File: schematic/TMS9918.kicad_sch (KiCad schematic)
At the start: 23 parts, among them J1 Bus, J2 Video out, J3 Power, J4 ext, Q1 2N4401, U1 TMS9918A, U2 HM62256BLP, U3 74HCT574, U4 74HCT574, U5 74HCT574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

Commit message: V1.1
Various improvements
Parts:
- removed A1: Arduino_Nano_v3.x, Module:Arduino_Nano, symbol MCU_Module:Arduino_Nano_v3.x
- removed C9: 0.1uf, Capacitor_THT:C_Disc_D3.0mm_W1.6mm_P2.50mm, symbol Device:C
- added R1: (no value), symbol Device:R
- C7, C8: value (none) -> 22pf
- J1: value Bus -> (none); footprint Connector_PinHeader_2.54mm:PinHeader_1x12_P2.54mm_Vertical -> (none)
- J4: value ext -> (none); footprint Connector_PinHeader_2.54mm:PinHeader_1x04_P2.54mm_Vertical -> (none)
- Q1: value 2N4401 -> (none); footprint Package_TO_SOT_THT:TO-92 -> (none)
- R3: value 470 -> (none)
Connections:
- net D0: now also U1.24 (CD0); no longer U1.17 (CD7)
- net D1: now also U1.23 (CD1); no longer U1.18 (CD6)
- net D2: now also U1.22 (CD2); no longer U1.19 (CD5)
- net D3: now also U1.21 (CD3); no longer U1.20 (CD4)
- net D4: now also U1.20 (CD4); no longer U1.21 (CD3)
- net D5: now also U1.19 (CD5); no longer U1.22 (CD2)
- net D6: now also U1.18 (CD6); no longer U1.23 (CD1)
- net D7: now also U1.17 (CD7); no longer U1.24 (CD0)
- net GND: now also R1.2
- net at J2.2 (Pin_2), Q1.1 (E): now also R1.1
- net COMVID renamed vid
- net CPUCLK: no longer names the net of J4.4 (Pin_4), U1.38 (CPUCLK)
- net EXTVDP renamed EXT
- net GROMCLK: no longer names the net of J4.3 (Pin_3), U1.37 (GROMCLK)
- net ~{INT}: no longer names the net of U1.16 (~{INT})
- no-connect marks 9 -> 5
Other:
- moved on the sheet: C2, C3, C4, C5, C6, U2, U3, U4, U5, U6D, U6E, U6F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

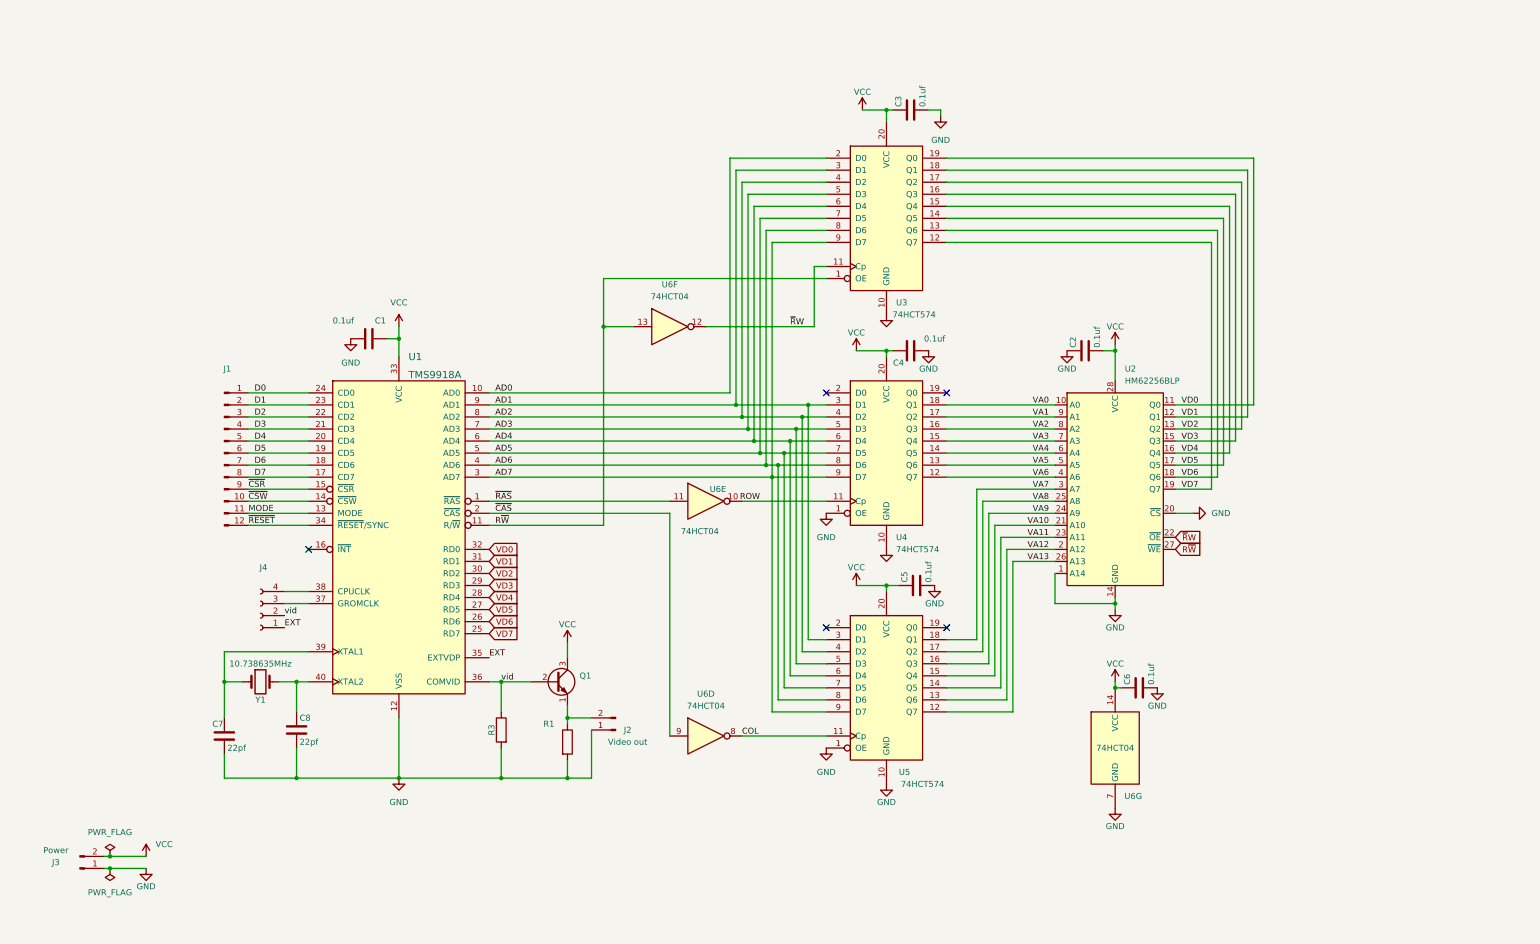
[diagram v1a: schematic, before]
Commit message: V1.2
Label D0..D7 order changed
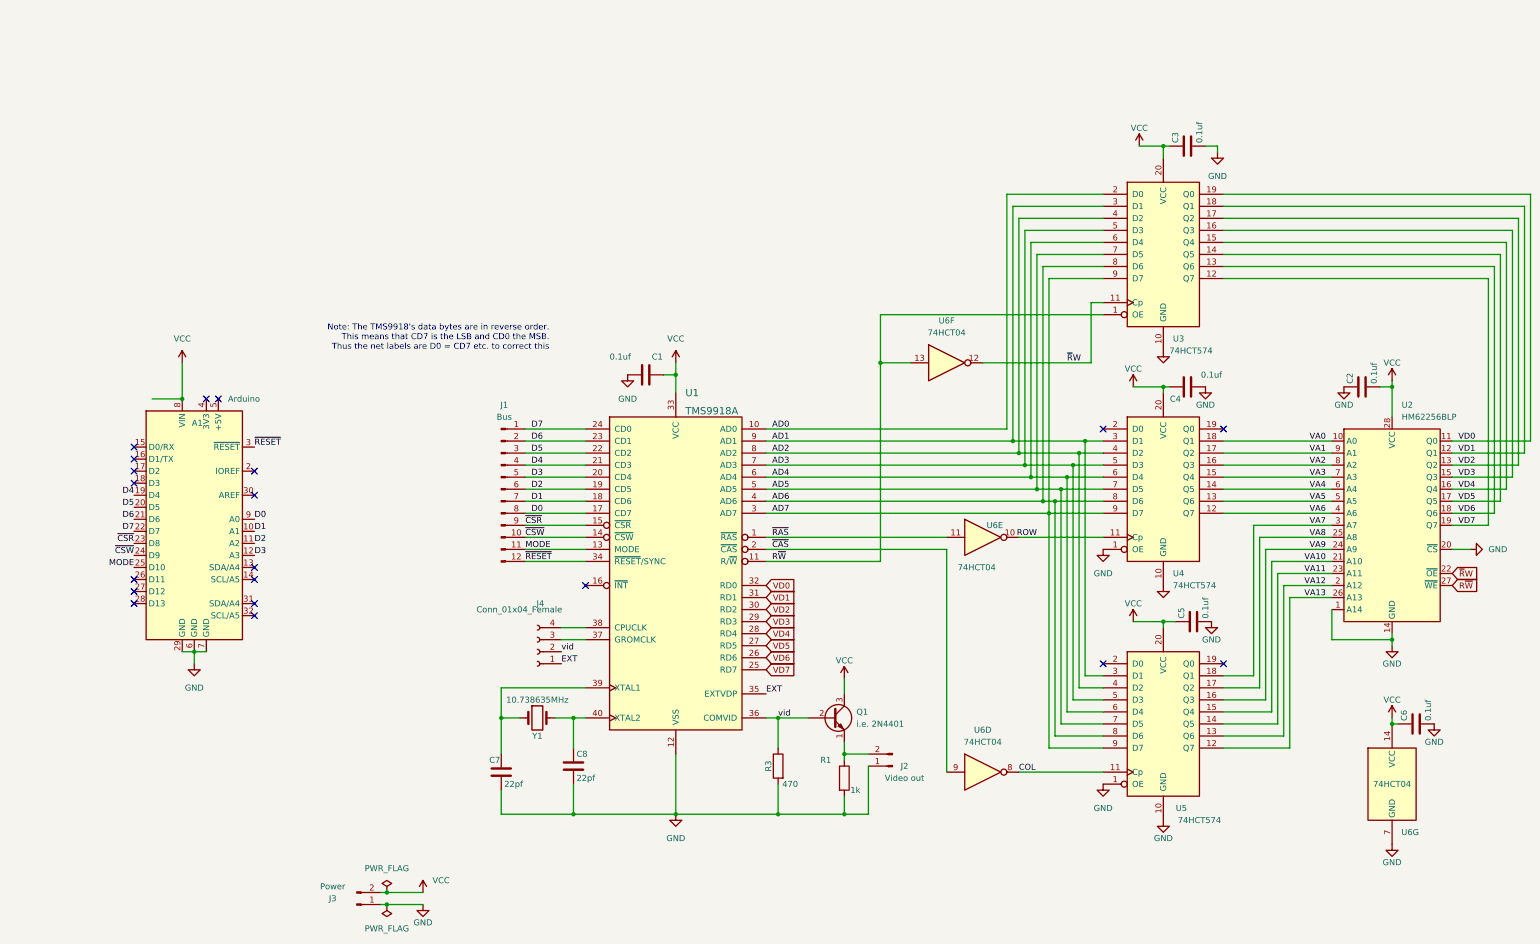
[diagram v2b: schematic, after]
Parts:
- added A1: Arduino, Module:Arduino_UNO_R3, symbol MCU_Module:Arduino_UNO_R3
- J1: value (none) -> Bus; footprint (none) -> Connector_PinHeader_2.54mm:PinHeader_1x12_P2.54mm_Vertical
- J4: value (none) -> Conn_01x04_Female; footprint (none) -> Connector_PinHeader_2.54mm:PinHeader_1x04_P2.54mm_Vertical
- Q1: value (none) -> i.e. 2N4401; footprint (none) -> Package_TO_SOT_THT:TO-92
- R1: value (none) -> 1k; footprint (none) -> Resistor_THT:R_Axial_DIN0207_L6.3mm_D2.5mm_P7.62mm_Horizontal
- R3: value (none) -> 470
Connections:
- net D0: now also J1.8 (Pin_8), U1.17 (CD7), A1.9 (A0); no longer J1.1 (Pin_1), U1.24 (CD0)
- net D1: now also J1.7 (Pin_7), U1.18 (CD6), A1.10 (A1); no longer J1.2 (Pin_2), U1.23 (CD1)
- net D2: now also J1.6 (Pin_6), U1.19 (CD5), A1.11 (A2); no longer J1.3 (Pin_3), U1.22 (CD2)
- net D3: now also J1.5 (Pin_5), U1.20 (CD4), A1.12 (A3); no longer J1.4 (Pin_4), U1.21 (CD3)
- net D4: now also J1.4 (Pin_4), U1.21 (CD3), A1.19 (D4); no longer J1.5 (Pin_5), U1.20 (CD4)
- net D5: now also J1.3 (Pin_3), U1.22 (CD2), A1.20 (D5); no longer J1.6 (Pin_6), U1.19 (CD5)
- net D6: now also J1.2 (Pin_2), U1.23 (CD1), A1.21 (D6); no longer J1.7 (Pin_7), U1.18 (CD6)
- net D7: now also J1.1 (Pin_1), U1.24 (CD0), A1.22 (D7); no longer J1.8 (Pin_8), U1.17 (CD7)
- net GND: now also A1.29 (GND), A1.6 (GND), A1.7 (GND)
- net MODE: now also A1.25 (D10)
- net VCC: now also A1.8 (VIN)
- net ~{CSR}: now also A1.23 (D8)
- net ~{CSW}: now also A1.24 (D9)
- net ~{RESET}: now also A1.3 (~{RESET})
- no-connect marks 5 -> 20
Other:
- note added: "Note: The TMS9918's data bytes are in reverse order. This means that CD7 is the LSB and CD0 the MSB. Thus the net labels are D0 = CD7 etc. to correct this"
- moved on the sheet: C1, C2, C3, C4, C5, C6, C7, C8, J1, J2, J3, J4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

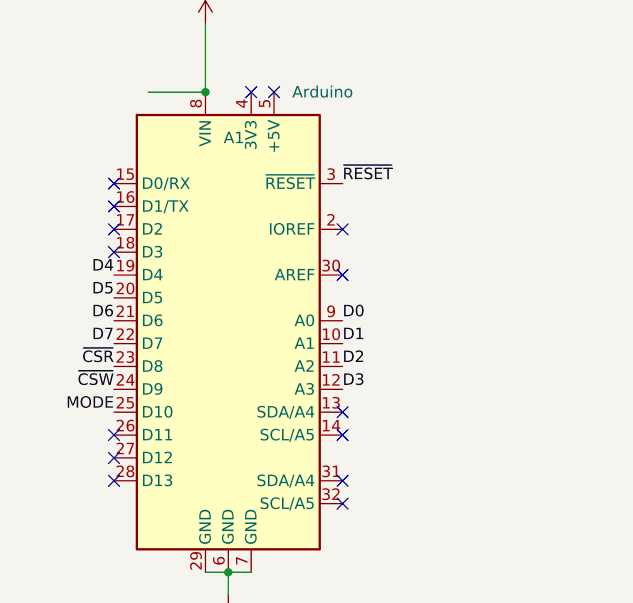
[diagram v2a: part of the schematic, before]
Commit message: V1.2
Wiring error Pin 8-11 between Arduino and module fixed
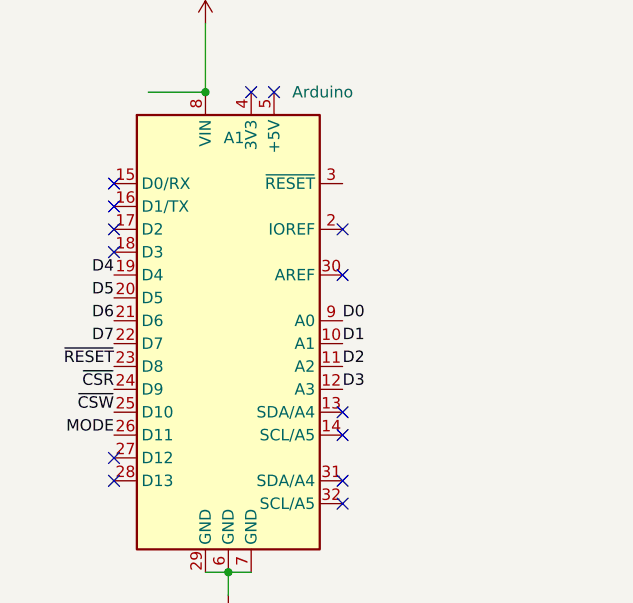
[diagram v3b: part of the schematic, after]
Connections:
- net MODE: now also A1.26 (D11); no longer A1.25 (D10)
- net ~{CSR}: now also A1.24 (D9); no longer A1.23 (D8)
- net ~{CSW}: now also A1.25 (D10); no longer A1.24 (D9)
- net ~{RESET}: now also A1.23 (D8); no longer A1.3 (~{RESET})
- no-connect marks 20 -> 19
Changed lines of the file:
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@@
     (title "TMS9918A ")
     (date "2022-03")
-    (rev "Rev.1.1")
+    (rev "Rev.1.2")
     (company "Doctor Volt")
   )
@@
   (no_connect (at 274.32 153.67))
   (no_connect (at 248.92 104.14))
-  (no_connect (at 44.45 135.89))
   (no_connect (at 44.45 138.43))
   (no_connect (at 44.45 140.97))
@@
     (effects (font (size 1.27 1.27)) (justify right bottom))
   )
-  (label "~{RESET}" (at 69.85 107.95 0)
-    (effects (font (size 1.27 1.27)) (justify left bottom))
+  (label "~{RESET}" (at 44.45 128.27 180)
+    (effects (font (size 1.27 1.27)) (justify right bottom))
   )
   (label "D5" (at 128.27 109.22 0)
@@
     (effects (font (size 1.27 1.27)) (justify left bottom))
   )
-  (label "MODE" (at 44.45 133.35 180)
+  (label "MODE" (at 44.45 135.89 180)
     (effects (font (size 1.27 1.27)) (justify right bottom))
   )
@@
     (effects (font (size 1.27 1.27)) (justify right bottom))
   )
-  (label "~{CSW}" (at 44.45 130.81 180)
+  (label "~{CSW}" (at 44.45 133.35 180)
     (effects (font (size 1.27 1.27)) (justify right bottom))
   )
-  (label "~{CSR}" (at 44.45 128.27 180)
+  (label "~{CSR}" (at 44.45 130.81 180)
     (effects (font (size 1.27 1.27)) (justify right bottom))
   )
